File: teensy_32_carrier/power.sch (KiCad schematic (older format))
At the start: 30 parts, among them P2 CONN_01X02, P3 CONN_01X02, Q1 STL62P3LLH6, SW3 MF-SW-TACT-6MM, SW4 MF-SW-TACT-6MM, U3 MF-DSC-SOT223-BSS138, U4 MF-DSC-SOT223-BSS138, U5 LMR14050

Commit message: first batch of layout
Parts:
- added D6: 1727-5317-1-ND, teensy:SOD-128, symbol D_Schottky_Small
- added J14: CJ, teensy:CJ-2, symbol CJ
- added J9: CON_01X05_PTH_2.54MM, MF_Connectors:MF_Connectors-PTH_2.54MM_01X05, symbol CON_01X05_PTH_2.54MM
- added R17: MF-RES-0402-10K, MF_Passives:MF_Passives-R0402, symbol RESISTOR_0402
- C10, C12, C7, C8, C9: footprint MF_Passives_C1210 -> MF_Passives:MF_Passives-C1210
- C11: footprint MF_Passives_CP10MM -> MF_Passives:MF_Passives-CP10MM
- C4: footprint MF_Passives_CP6.3MM -> MF_Passives:MF_Passives-CP6.3MM
- C5: footprint MF_Passives_C0402 -> MF_Passives:MF_Passives-C0402
- C6: footprint MF_Passives_C0603 -> MF_Passives:MF_Passives-C0603
- R11: value 311-127KHRCT-ND -> MF-RES-0402-100K; footprint MF_Passives:MF_Passives-R0603 -> MF_Passives:MF_Passives-R0402
- R12: value 1276-4773-1-ND -> 311-17.4KLRCT-ND; footprint MF_Passives:MF_Passives-R0603 -> MF_Passives:MF_Passives-R0402
- R15: value MF-RES-0603-255K -> MF-RES-0402-100K; footprint MF_Passives:MF_Passives-R0603 -> MF_Passives:MF_Passives-R0402
- R16: value 311-56KHRCT-ND -> 311-14.0KLRCT-ND; footprint MF_Passives:MF_Passives-R0603 -> MF_Passives:MF_Passives-R0402
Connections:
- net +5V: now also J14.1, J9.3 (PIN3)
- net +BATT: now also P3.1 (P1), D6.2 (A); no longer C12.1, C4.1, P3.2 (P2), U5.2 (VIN)
- net GND: now also P2.2 (P2), P3.2 (P2), J9.1 (PIN1); no longer P2.1 (P1), P3.1 (P1)
- net PWRON2: now also R17.2
- net VR_BT: now reaches C6.1, U5.1 (BOOT)
- net VR_EN: now reaches R15.2, R16.1, U5.3 (EN)
- net VR_RT: now reaches R10.1, U5.4 (RT/SYNC)
- net VR_FB: now reaches R11.2, R12.1, U5.5 (FB)
- net VR_SS: now reaches C5.1, U5.6 (SS)
- net VR_SW: now reaches C6.2, D3.1 (K), L1.2, U5.8 (SW)
- net BAT_IN: now reaches C3.1, D2.1 (K), Q1.1 (S), R8.1, SW3.2
- net BAT_IN: now also P2.1 (P1), J9.5 (PIN5); no longer P2.2 (P2)
- net OFF_NODE: now reaches D2.2 (A), Q1.2 (G), R8.2, R9.1, SW3.4
- net OFF_NODE: now also J9.4 (PIN4)
- net ON_NODE: now reaches R9.2, SW4.1, U3.3 (DRAIN), U4.3 (DRAIN)
- net ON_NODE: now also J9.2 (PIN2)
- new net: J14.2, R17.1
- new net VR_VI: C12.1, C4.1, D6.1 (K), U5.2 (VIN)
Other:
- note added: "Enough capacitance with low enough ESR\nand significant margin above 450 kHz fSW."
- note added: "Keep board on once on, \nunless Teensy forces it off"
- note added: "Prevent ESC from draining\nbuck converter input caps"
- note added: "Turn on at 6V, turn off at 5.7V\nwhich works with 6.2V NiMH.\nMay be too low to protect 2S"
- note removed: "Enough capacitance with low enough ESR\nand significant margin above 600 kHz fSW."
- note removed: "Turn on at 7V, turn off at 6.1V\nwhich is enough to protect 2S"
- moved on the sheet: C12, C4, R15, R16

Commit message: Choose a part for screw terminals.
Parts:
- P2, P3: value CONN_01X02 -> A98159-ND
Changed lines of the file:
@@
 P 1300 2250
 F 0 "P2" H 1300 2400 50  0000 C CNN
-F 1 "CONN_01X02" V 1400 2250 50  0000 C CNN
+F 1 "A98159-ND" V 1400 2250 50  0000 C CNN
 F 2 "teensy:SCREW-3.5MM" H 1300 2250 50  0001 C CNN
 F 3 "" H 1300 2250 50  0000 C CNN
@@
 P 8200 2250
 F 0 "P3" H 8200 2400 50  0000 C CNN
-F 1 "CONN_01X02" V 8300 2250 50  0000 C CNN
+F 1 "A98159-ND" V 8300 2250 50  0000 C CNN
 F 2 "teensy:SCREW-3.5MM" H 8200 2250 50  0001 C CNN
 F 3 "" H 8200 2250 50  0000 C CNN

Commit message: prep for order v0.1
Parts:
- C12: value 311-2054-1-ND -> 311-3532-1-ND
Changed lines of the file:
@@
 P 5500 3250
 F 0 "C12" V 5450 3050 45  0000 L BNN
-F 1 "311-2054-1-ND" V 5650 3050 45  0000 L BNN
+F 1 "311-3532-1-ND" V 5650 3050 45  0000 L BNN
 F 2 "MF_Passives:MF_Passives-C1210" H 5750 3160 20  0001 C CNN
 F 3 "" H 5500 3250 60  0001 C CNN

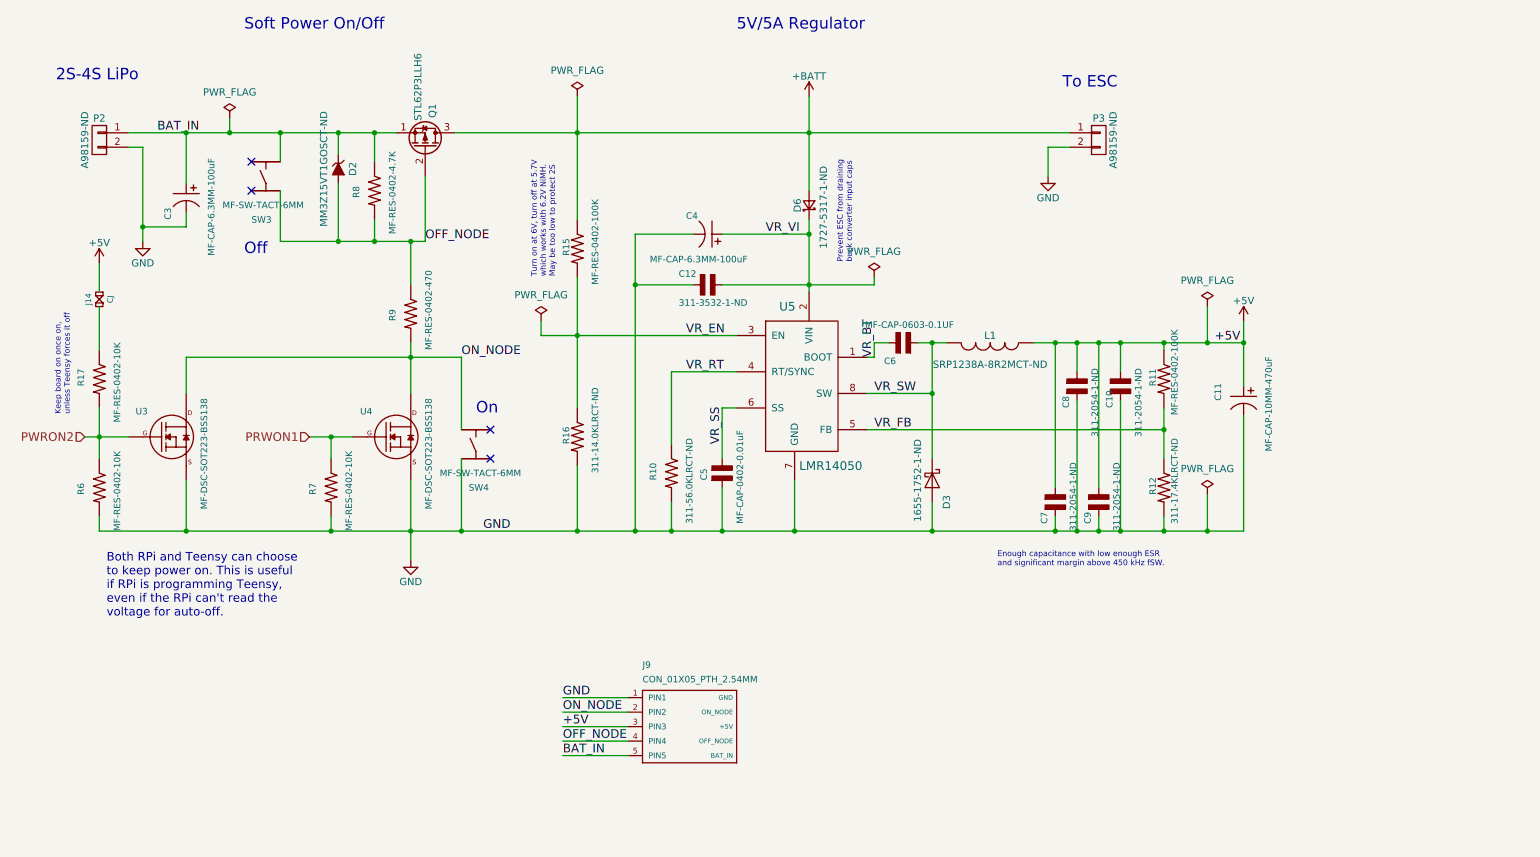
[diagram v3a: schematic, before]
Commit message: trying to fit an RTC and the Hat EEPROM, but no.
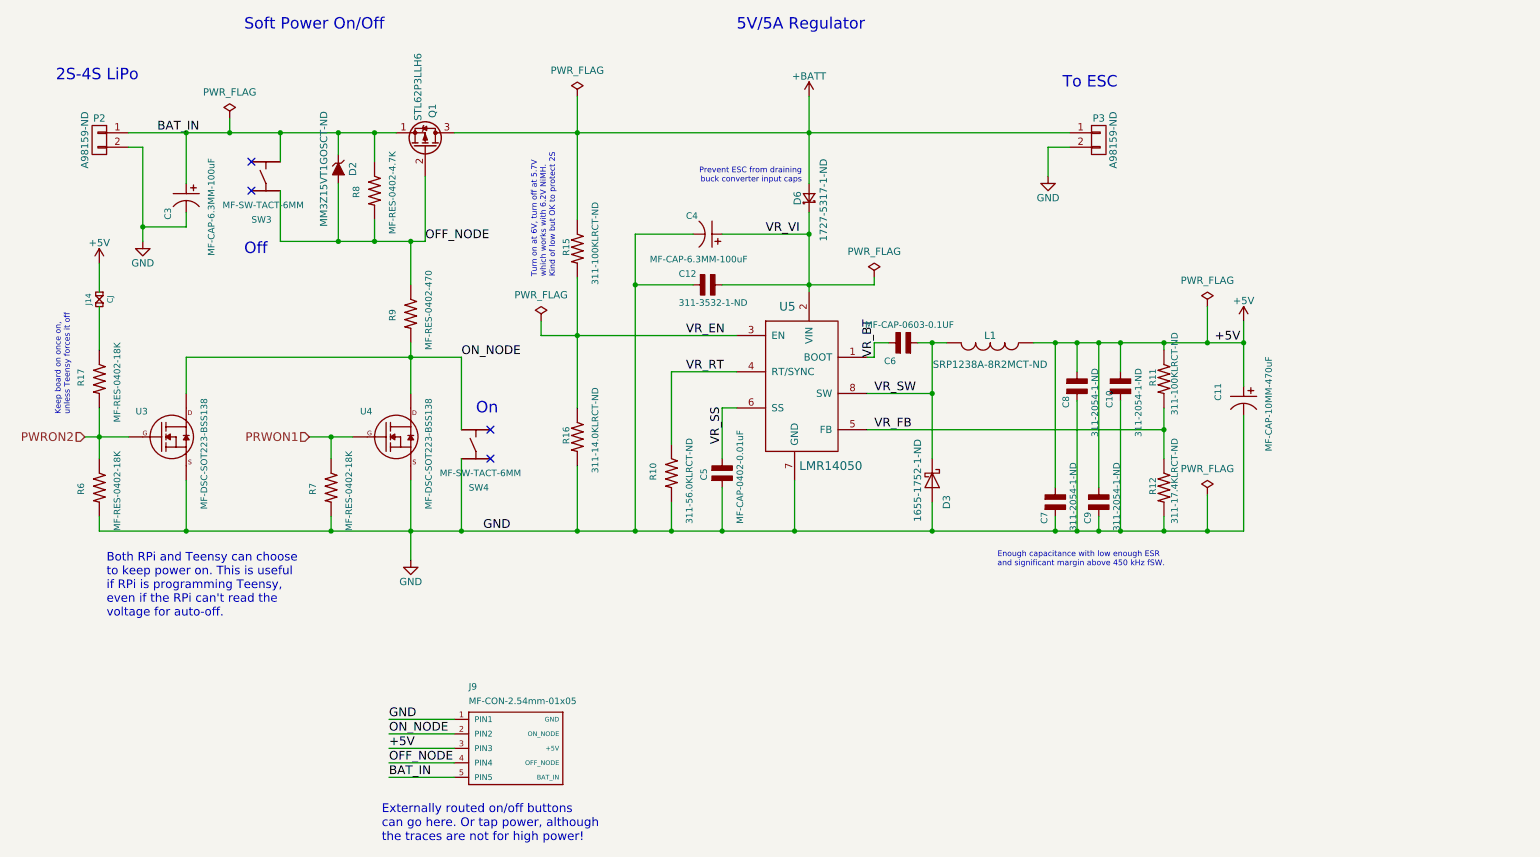
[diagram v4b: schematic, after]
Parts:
- J9: value CON_01X05_PTH_2.54MM -> MF-CON-2.54mm-01x05
- R11, R15: value MF-RES-0402-100K -> 311-100KLRCT-ND
- R17, R6, R7: value MF-RES-0402-10K -> MF-RES-0402-18K
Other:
- note added: "Externally routed on/off buttons\ncan go here. Or tap power, although\nthe traces are not for high power!"
- note added: "Turn on at 6V, turn off at 5.7V\nwhich works with 6.2V NiMH.\nKind of low but OK to protect 2S"
- note removed: "Turn on at 6V, turn off at 5.7V\nwhich works with 6.2V NiMH.\nMay be too low to protect 2S"
- moved on the sheet: D6, J9
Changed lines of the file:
@@
 P 2900 4650
 F 0 "R7" V 2800 4600 45  0000 L BNN
-F 1 "MF-RES-0402-10K" V 3050 4350 45  0000 L BNN
+F 1 "MF-RES-0402-18K" V 3050 4350 45  0000 L BNN
 F 2 "MF_Passives:MF_Passives-R0402" H 3150 4560 20  0001 C CNN
 F 3 "" H 2900 4650 60  0001 C CNN
@@
 P 1300 4650
 F 0 "R6" V 1200 4600 45  0000 L BNN
-F 1 "MF-RES-0402-10K" V 1450 4350 45  0000 L BNN
+F 1 "MF-RES-0402-18K" V 1450 4350 45  0000 L BNN
 F 2 "MF_Passives:MF_Passives-R0402" H 1550 4560 20  0001 C CNN
 F 3 "" H 1300 4650 60  0001 C CNN
@@
 P 8650 3900
 F 0 "R11" V 8600 3850 45  0000 L BNN
-F 1 "MF-RES-0402-100K" V 8750 3650 45  0000 L BNN
+F 1 "311-100KLRCT-ND" V 8750 3650 45  0000 L BNN
 F 2 "MF_Passives:MF_Passives-R0402" H 8900 3810 20  0001 C CNN
 F 3 "" H 8650 3900 60  0001 C CNN
@@
 P 4600 3000
 F 0 "R15" V 4550 2950 45  0000 L BNN
-F 1 "MF-RES-0402-100K" V 4750 2750 45  0000 L BNN
+F 1 "311-100KLRCT-ND" V 4750 2750 45  0000 L BNN
 F 2 "MF_Passives:MF_Passives-R0402" H 4850 2910 20  0001 C CNN
 F 3 "" H 4600 3000 60  0001 C CNN
@@
 Connection ~ 2950 2950
 Text Notes 4450 3200 1    39   ~ 0
-Turn on at 6V, turn off at 5.7V\nwhich works with 6.2V NiMH.\nMay be too low to protect 2S
+Turn on at 6V, turn off at 5.7V\nwhich works with 6.2V NiMH.\nKind of low but OK to protect 2S
 Text Notes 7500 5200 0    39   ~ 0
 Enough capacitance with low enough ESR\nand significant margin above 450 kHz fSW.
@@
 GND
 Wire Wire Line
-	4950 6100 4500 6100
-Wire Wire Line
-	4950 6200 4500 6200
-Wire Wire Line
-	4950 6400 4500 6400
-Wire Wire Line
-	4950 6500 4500 6500
-Text Label 4500 6100 0    60   ~ 0
+	3750 6250 3300 6250
+Wire Wire Line
+	3750 6350 3300 6350
+Wire Wire Line
+	3750 6550 3300 6550
+Wire Wire Line
+	3750 6650 3300 6650
+Text Label 3300 6250 0    60   ~ 0
 GND
-Text Label 4500 6200 0    60   ~ 0
+Text Label 3300 6350 0    60   ~ 0
 ON_NODE
-Text Label 4500 6400 0    60   ~ 0
+Text Label 3300 6550 0    60   ~ 0
 OFF_NODE
-Text Label 4500 6500 0    60   ~ 0
+Text Label 3300 6650 0    60   ~ 0
 BAT_IN
 Text Label 9000 3650 0    60   ~ 0
 +5V
 Wire Wire Line
-	4500 6300 4950 6300
-Text Label 4500 6300 0    60   ~ 0
+	3300 6450 3750 6450
+Text Label 3300 6450 0    60   ~ 0
 +5V
 $Comp
 L CON_01X05_PTH_2.54MM J9
 U 1 1 59968E5E
-P 5050 6100
-F 0 "J9" H 5050 6300 45  0000 L BNN
-F 1 "CON_01X05_PTH_2.54MM" H 5050 6200 45  0000 L BNN
-F 2 "MF_Connectors:MF_Connectors-PTH_2.54MM_01X05" H 5375 5615 20  0001 C CNN
-F 3 "" H 5050 6100 60  0000 C CNN
-F 4 "GND" H 5675 6100 32  0000 R CNN "LABEL01"
-F 5 "ON_NODE" H 5675 6000 32  0000 R CNN "LABEL02"
-F 6 "+5V" H 5675 5900 32  0000 R CNN "LABEL03"
-F 7 "OFF_NODE" H 5675 5800 32  0000 R CNN "LABEL04"
-F 8 "BAT_IN" H 5675 5700 32  0000 R CNN "LABEL05"
-	1    5050 6100
+P 3850 6250
+F 0 "J9" H 3850 6450 45  0000 L BNN
+F 1 "MF-CON-2.54mm-01x05" H 3850 6350 45  0000 L BNN
+F 2 "MF_Connectors:MF_Connectors-PTH_2.54MM_01X05" H 4175 5765 20  0001 C CNN
+F 3 "" H 3850 6250 60  0000 C CNN
+F 4 "GND" H 4475 6250 32  0000 R CNN "LABEL01"
+F 5 "ON_NODE" H 4475 6150 32  0000 R CNN "LABEL02"
+F 6 "+5V" H 4475 6050 32  0000 R CNN "LABEL03"
+F 7 "OFF_NODE" H 4475 5950 32  0000 R CNN "LABEL04"
+F 8 "BAT_IN" H 4475 5850 32  0000 R CNN "LABEL05"
+	1    3850 6250
 	1    0    0    -1
 $EndComp
@@
 L D_Schottky_Small D6
 U 1 1 5996460F
-P 6200 2700
-F 0 "D6" H 6150 2780 50  0000 L CNN
-F 1 "1727-5317-1-ND" H 5900 2600 50  0000 L CNN
-F 2 "teensy:SOD-128" V 6200 2700 50  0001 C CNN
-F 3 "" V 6200 2700 50  0000 C CNN
-	1    6200 2700
+P 6200 2650
+F 0 "D6" H 6150 2730 50  0000 L CNN
+F 1 "1727-5317-1-ND" H 5900 2550 50  0000 L CNN
+F 2 "teensy:SOD-128" V 6200 2650 50  0001 C CNN
+F 3 "" V 6200 2650 50  0000 C CNN
+	1    6200 2650
 	0    -1   -1   0
 $EndComp
 Wire Wire Line
-	6200 1950 6200 2600
-Wire Wire Line
-	6200 2800 6200 3300
+	6200 1950 6200 2550
+Wire Wire Line
+	6200 2750 6200 3300
 Wire Wire Line
 	5000 2900 5000 4950
@@
 P 1300 3900
 F 0 "R17" V 1200 3850 45  0000 L BNN
-F 1 "MF-RES-0402-10K" V 1450 3600 45  0000 L BNN
+F 1 "MF-RES-0402-18K" V 1450 3600 45  0000 L BNN
 F 2 "MF_Passives:MF_Passives-R0402" H 1550 3810 20  0001 C CNN
 F 3 "" H 1300 3900 60  0001 C CNN
@@
 	1    0    0    -1
 $EndComp
-Text Notes 6500 3100 1    39   ~ 0
+Text Notes 6150 2550 2    39   ~ 0
 Prevent ESC from draining\nbuck converter input caps
 Text Notes 1100 4150 1    39   ~ 0
@@
 Text Label 5900 2900 0    60   ~ 0
 VR_VI
+Text Notes 3250 7100 0    60   ~ 0
+Externally routed on/off buttons\ncan go here. Or tap power, although\nthe traces are not for high power!
 $EndSCHEMATC

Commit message: version 2 macrofab project
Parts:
- added J16: CON_01X04_PTH_2.54MM, MF_Connectors:MF_Connectors-PTH_2.54MM_01X04, symbol CON_01X04_PTH_2.54MM
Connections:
- net +5V: now also J16.1 (PIN1), J16.3 (PIN3)
- net GND: now also J16.2 (PIN2), J16.4 (PIN4)
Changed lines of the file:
@@
 $Descr A4 11693 8268
 encoding utf-8
-Sheet 2 2
+Sheet 2 3
 Title ""
 Date ""
@@
 	3800 4950 3800 4450
 Wire Wire Line
-	1300 4950 9200 4950
+	1300 4950 9900 4950
 Wire Wire Line
 	3450 4600 3450 5150
@@
 	8650 3650 8650 3700
 Wire Wire Line
-	7750 3650 9200 3650
+	7750 3650 9750 3650
 Wire Wire Line
 	9200 3500 9200 3950
@@
 Text Notes 3250 7100 0    60   ~ 0
 Externally routed on/off buttons\ncan go here. Or tap power, although\nthe traces are not for high power!
+$Comp
+L CON_01X04_PTH_2.54MM J16
+U 1 1 59BA13A4
+P 10200 4050
+F 0 "J16" H 10200 4250 45  0000 L BNN
+F 1 "CON_01X04_PTH_2.54MM" H 10200 4150 45  0000 L BNN
+F 2 "MF_Connectors:MF_Connectors-PTH_2.54MM_01X04" H 10525 3665 20  0001 C CNN
+F 3 "" H 10200 4050 60  0000 C CNN
+F 4 "+5V" H 10825 4050 32  0000 R CNN "LABEL01"
+F 5 "GND" H 10825 3950 32  0000 R CNN "LABEL02"
+F 6 "+5V" H 10825 3850 32  0000 R CNN "LABEL03"
+F 7 "GND" H 10825 3750 32  0000 R CNN "LABEL04"
+	1    10200 4050
+	1    0    0    -1
+$EndComp
+Wire Wire Line
+	10100 4050 9750 4050
+Wire Wire Line
+	9750 3650 9750 4250
+Wire Wire Line
+	9750 4250 10100 4250
+Connection ~ 9750 4050
+Wire Wire Line
+	10100 4150 9900 4150
+Wire Wire Line
+	9900 4150 9900 4950
+Connection ~ 9200 4950
+Wire Wire Line
+	10100 4350 9900 4350
+Connection ~ 9900 4350
 $EndSCHEMATC

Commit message: carrier update
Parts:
- C6: value MF-CAP-0603-0.1UF -> MF-CAP-0603-0.1uF
- J16: value CON_01X04_PTH_2.54MM -> MF-CON-2.54mm-01x04
- U3, U4: value MF-DSC-SOT223-BSS138 -> MF-DSC-SOT233-BSS138
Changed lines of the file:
@@
 P 3350 4300
 F 0 "U4" H 3100 4450 45  0000 L BNN
-F 1 "MF-DSC-SOT223-BSS138" V 3600 3800 45  0000 L BNN
+F 1 "MF-DSC-SOT233-BSS138" V 3600 3800 45  0000 L BNN
 F 2 "MF_Discrete_Semiconductor:MF_Discrete_Semiconductor-SOT-23-3" H 3848 4371 20  0001 C CNN
 F 3 "" H 3350 4300 60  0001 C CNN
@@
 P 1800 4300
 F 0 "U3" H 1550 4450 45  0000 L BNN
-F 1 "MF-DSC-SOT223-BSS138" V 2050 3800 45  0000 L BNN
+F 1 "MF-DSC-SOT233-BSS138" V 2050 3800 45  0000 L BNN
 F 2 "MF_Discrete_Semiconductor:MF_Discrete_Semiconductor-SOT-23-3" H 2298 4371 20  0001 C CNN
 F 3 "" H 1800 4300 60  0001 C CNN
@@
 P 6850 3650
 F 0 "C6" V 6750 3700 45  0000 L BNN
-F 1 "MF-CAP-0603-0.1UF" V 7000 3300 45  0000 L BNN
+F 1 "MF-CAP-0603-0.1uF" V 7000 3300 45  0000 L BNN
 F 2 "MF_Passives:MF_Passives-C0603" H 7100 3560 20  0001 C CNN
 F 3 "" H 6850 3650 60  0001 C CNN
@@
 P 10200 4050
 F 0 "J16" H 10200 4250 45  0000 L BNN
-F 1 "CON_01X04_PTH_2.54MM" H 10200 4150 45  0000 L BNN
+F 1 "MF-CON-2.54mm-01x04" H 10200 4150 45  0000 L BNN
 F 2 "MF_Connectors:MF_Connectors-PTH_2.54MM_01X04" H 10525 3665 20  0001 C CNN
 F 3 "" H 10200 4050 60  0000 C CNN
